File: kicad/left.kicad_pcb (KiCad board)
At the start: 4 copper layers, 127.3 x 89.6 mm, 139 parts, among them Q1 PMF170XP,115, Q2 FS8205A_C2830320, SW1 TS-1088-AR02016, U1 SN74LVC1G17DBVR, U2 E73-2G4M08S1C, U3 SN74LVC1G74DQER, U4 S2B-PH-K-S(LF)(SN), U5 BL8573CS8TR, U6 DW01A_C42380662, U7 LP5024RSMR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

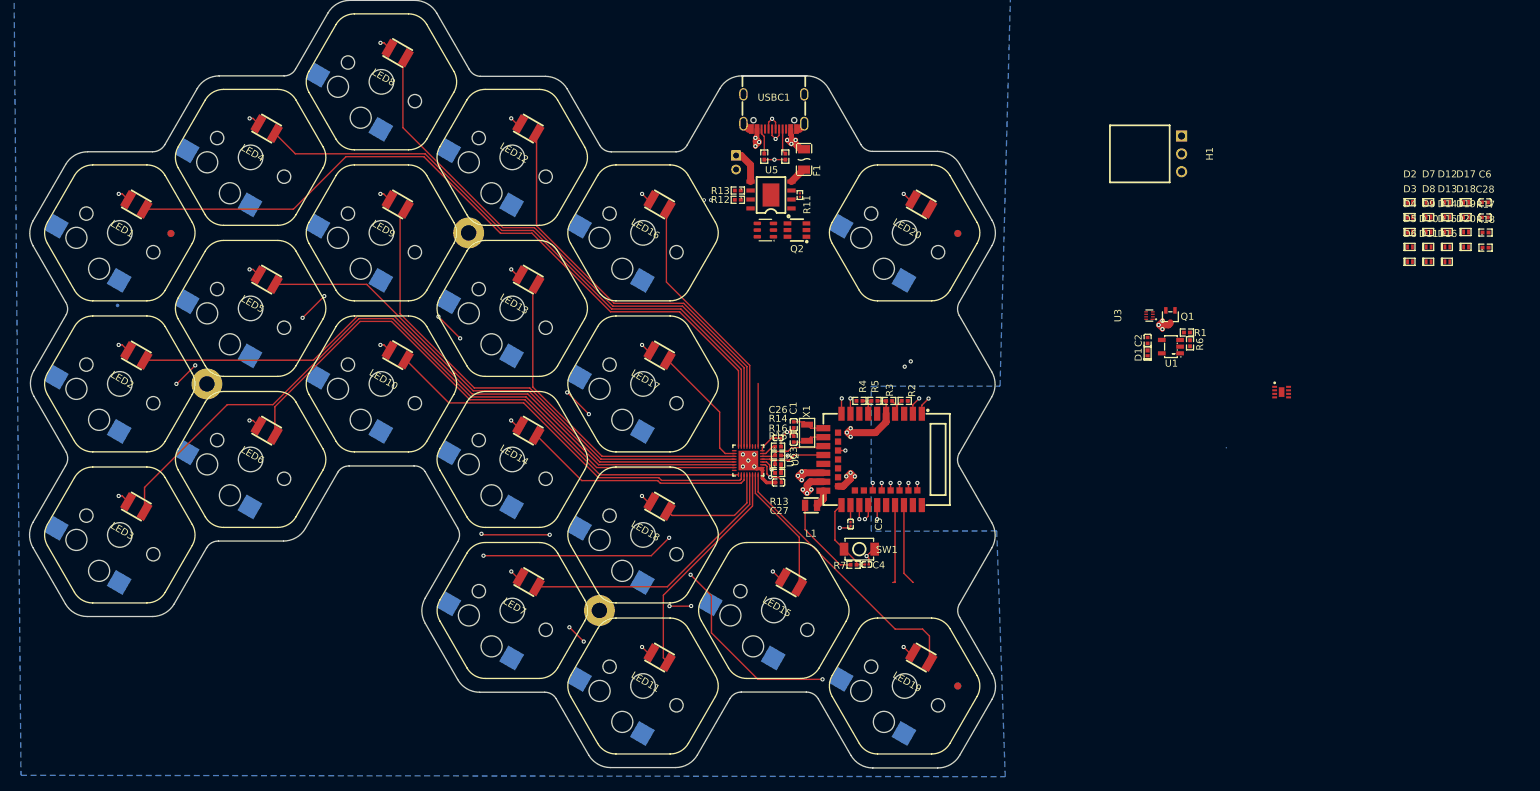
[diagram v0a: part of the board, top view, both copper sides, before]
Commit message: finished. needes inspection. added battery measurer. wired left side
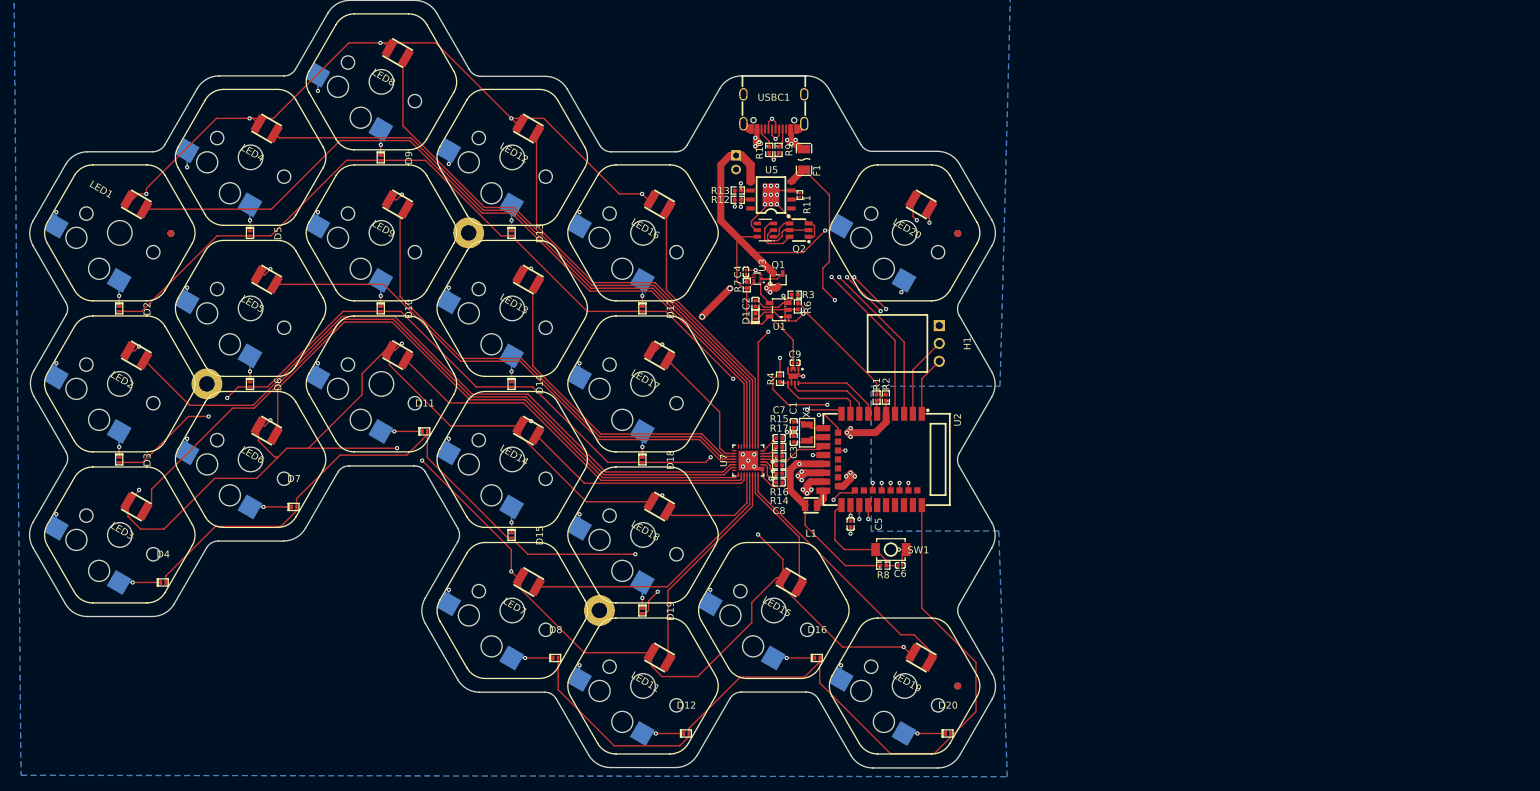
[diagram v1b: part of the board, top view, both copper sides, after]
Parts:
- removed C26: GRM033C71C104KE14D, easyeda2kicad:C0201
- removed C27, C28: GRM155C71C105KE11D, easyeda2kicad:C0402
- removed the R13 at (126.6, 83.1)
- removed R18: RC0402FR-0710KL, easyeda2kicad:R0402
- removed R5: RC0402FR-07100KL, easyeda2kicad:R0402
- added C7: GRM155C71C105KE11D, easyeda2kicad:C0402, F.Cu at (126.7, 78.1)
- added C8: GRM155C71C105KE11D, easyeda2kicad:C0402, F.Cu at (126.7, 84.4)
- added C9: GRM033C71C104KE14D, easyeda2kicad:C0201, F.Cu at (129.0, 67.4)
- added R10: RC0402FR-075K1L, easyeda2kicad:R0402, F.Cu at (125.3, 37.1)
- C5: footprint easyeda2kicad:C0201 -> easyeda2kicad:C0402
- C6: footprint easyeda2kicad:C0402 -> easyeda2kicad:C0201
- moved D3 187.0 mm to (32.8, 81.2), turned to -90 degrees
- moved D2 184.4 mm to (32.8, 59.7), turned to -90 degrees
- moved D4 184.3 mm to (39.1, 98.7)
- moved D7 167.2 mm to (57.7, 87.9)
- moved D6 166.0 mm to (51.4, 70.5), turned to -90 degrees
- moved D5 165.1 mm to (51.4, 49.0), turned to -90 degrees
- moved D9 149.5 mm to (70.0, 38.2), turned to -90 degrees
- moved D10 149.4 mm to (70.0, 59.7), turned to -90 degrees
- moved D11 144.9 mm to (76.3, 77.2)
- moved D15 139.4 mm to (88.6, 92.0), turned to -90 degrees
- moved D8 139.2 mm to (94.9, 109.4)
- moved D14 135.0 mm to (88.6, 70.5), turned to -90 degrees
- moved D13 133.2 mm to (88.6, 49.0), turned to -90 degrees
- moved D12 132.1 mm to (113.5, 120.2)
- moved D19 129.1 mm to (107.3, 102.7), turned to -90 degrees
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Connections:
- U2 pad 1: unconnected-(U2-P1.11-Pad1) -> /SWDIO
- U2 pad 10: /ROW2 -> /ROW1
- U2 pad 12: /ROW3 -> /ROW2
- U2 pad 18: /BAT_ALTR -> unconnected-(U2-AI2-Pad18)
- U2 pad 2: unconnected-(U2-P1.10-Pad2) -> /SWBCLK
- U2 pad 28: /ROW1 -> /ROW3
- U2 pad 3: unconnected-(U2-P0.03-Pad3) -> /STDBY
- U2 pad 30: /PWR_BTN_PRESS -> unconnected-(U2-P17-Pad30)
- U2 pad 32: /COL4 -> /COL5
- U2 pad 34: /COL3 -> /COL4
- U2 pad 36: /COL2 -> /COL3
- U2 pad 37: /SWDIO -> unconnected-(U2-SWD-Pad37)
- U2 pad 38: /COL1 -> /COL2
- U2 pad 39: /SWBCLK -> unconnected-(U2-SWC-Pad39)
- U2 pad 4: unconnected-(U2-AI4-Pad4) -> /CHRG
- U2 pad 40: unconnected-(U2-P1.04-Pad40) -> /COL1
- U2 pad 41: /CHRG -> unconnected-(U2-NF1-Pad41)
- U2 pad 43: /STDBY -> /ROW4
- U2 pad 6: /COL5 -> /PWR_BTN_PRESS
- U2 pad 7: unconnected-(U2-AI0-Pad7) -> /SDA_BAT
- U2 pad 8: unconnected-(U2-AI5-Pad8) -> /SCL_BAT
- U2 pad 9: /ROW4 -> /BAT_ALTR
- U7 pad 1: /LED19 -> /LED20
- U7 pad 10: /LED3 -> /LED17
- U7 pad 11: /LED2 -> /LED13
- U7 pad 12: /LED5 -> /LED9
- U7 pad 13: /LED9 -> /LED5
- U7 pad 14: /LED13 -> /LED2
- U7 pad 15: /LED17 -> /LED3
- U7 pad 17: /LED1 -> /LED6
- U7 pad 18: /LED4 -> /LED10
- U7 pad 19: /LED8 -> /LED14
- U7 pad 2: /LED15 -> /LED16
- U7 pad 20: /LED12 -> /LED18
- U7 pad 21: /LED16 -> /LED7
- U7 pad 22: /LED20 -> /LED11
- U7 pad 23: unconnected-(U7-OUT22-Pad23) -> /LED15
- U7 pad 24: unconnected-(U7-OUT23-Pad24) -> /LED19
- U7 pad 3: /LED11 -> /LED12
- U7 pad 4: /LED7 -> /LED8
- U7 pad 5: /LED18 -> /LED4
- U7 pad 6: /LED14 -> /LED1
- U7 pad 7: /LED10 -> unconnected-(U7-OUT6-Pad7)
- U7 pad 8: /LED6 -> unconnected-(U7-OUT7-Pad8)
- U8 pad 7: /SCL -> /SCL_BAT
- U8 pad 8: /SDA -> /SDA_BAT
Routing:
- net /PWR: track 47.6 -> 694.1 mm, vias 27 -> 30
- net /COL5: track 0.00 -> 184.1 mm, vias 0 -> 5
- net unconnected-(U2-P0.13-Pad33): track 135.4 -> 0.00 mm, vias 3 -> 0
- net /ROW3: track 0.00 -> 131.9 mm, vias 0 -> 3
- net unconnected-(U2-P1.04-Pad40): track 126.8 -> 0.00 mm, vias 3 -> 0
- net /ROW1: track 0.00 -> 126.7 mm, vias 0 -> 2
- net unconnected-(U2-P1.06-Pad42): track 109.7 -> 0.00 mm, vias 1 -> 0
- net /COL1: track 130.8 -> 228.3 mm, vias 3 -> 4
- net /COL2: track 166.7 -> 255.9 mm, vias 1 -> 5
- net /VDD_nRF: track 14.2 -> 87.9 mm, vias 1 -> 4
- net /COL3: track 164.0 -> 232.0 mm, vias 3 -> 5
- net /BAT+: track 5.00 -> 72.1 mm, vias 0 -> 1
- net /VBUS: track 4.50 -> 68.4 mm, vias 0 -> 2
- net /ROW4: track 177.6 -> 116.6 mm, vias 1 -> 0
- net /LED20: track 2.35 -> 51.7 mm, vias 0 -> 2
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
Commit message: changed on/off timing resistor to 2M61 0805
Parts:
- removed R6: 0402WGF1604TCE, easyeda2kicad:R0402
- added R5: RC0805FR-072M61L, easyeda2kicad:R0805, F.Cu at (131.2, 60.9)
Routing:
- net GND: track 85.3 -> 81.0 mm, vias 30 -> 31
- net Net-(U1-A): track 6.99 -> 9.84 mm
- net /PWR_BTN: track 44.6 -> 46.8 mm

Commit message: added gnd vias all over the board. went trough schematic again. changed resistor for rc to bigger one in footprint, and smaller one in Ohm. both left and right sides are ready. just need to go over the kicads check and lastly let someone on discord have a look on the project
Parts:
- removed Fi4, Fi5: Fiducial_1mm_Mask2mm, Fiducial:Fiducial_1mm_Mask2mm
- removed Fi6: Fiducial_1mm_Mask2mm, 
- removed G*** (x2): LOGO, images:monster
- removed R15: RT0402BRD0737K4L, easyeda2kicad:R0402
- added BAT+: TestPoint_Pad_D1.5mm, TestPoint:TestPoint_Pad_D1.5mm, F.Cu at (118.3, 36.1)
- added GND: TestPoint_Pad_D1.5mm, TestPoint:TestPoint_Pad_D1.5mm, F.Cu at (116.5, 39.6)
- added PWR: TestPoint_Pad_D1.5mm, TestPoint:TestPoint_Pad_D1.5mm, F.Cu at (116.6, 57.6)
- added R6: ERA2AED753X, easyeda2kicad:R0402, F.Cu at (126.7, 79.4)
- added VBUS: TestPoint_Pad_D1.5mm, TestPoint:TestPoint_Pad_D1.5mm, F.Cu at (134.6, 40.1)
- added VDD_nrf: TestPoint_Pad_D1.5mm, TestPoint:TestPoint_Pad_D1.5mm, F.Cu at (126.0, 65.0)
- G**: moved to B.Cu
- moved G** 296.4 mm to (127.1, 68.4), turned to 180 degrees
- moved Fi2 2.00 mm to (42.2, 49.0)
- moved Fi1 1.00 mm to (153.2, 49.0)
- moved Fi3 1.00 mm to (153.2, 113.4)
- moved D1 0.19 mm to (123.4, 61.0)
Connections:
- U6 pad 5: GND -> /BAT+
- U6 pad 6: /BAT+ -> GND
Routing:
- net /PWR: track 694.1 -> 701.5 mm
- net GND: track 81.0 -> 85.5 mm, vias 31 -> 97
- net /VBUS: track 68.4 -> 72.8 mm
- net /BAT+: track 72.1 -> 75.6 mm
- net /VDD_nRF: track 87.9 -> 90.4 mm
- net /LED1: track 112.7 -> 115.0 mm
- net /COL2: track 255.9 -> 257.7 mm
- net /COL1: track 228.3 -> 229.5 mm
- net /COL3: track 232.0 -> 233.2 mm
- net /LED12: track 62.5 -> 61.8 mm
- net /LED3: track 106.1 -> 105.5 mm
- net /LED2: track 101.4 -> 100.9 mm

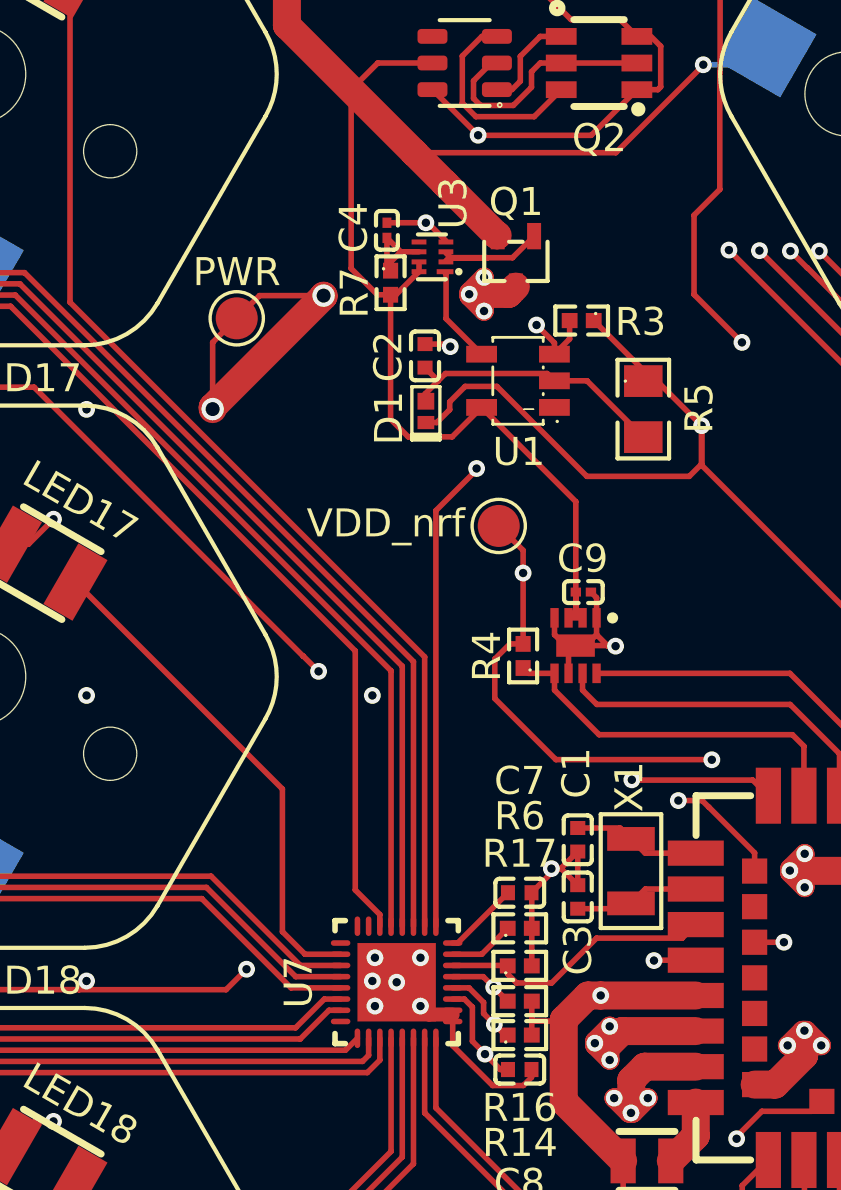
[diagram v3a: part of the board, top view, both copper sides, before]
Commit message: update vias under led controller... on left part. checking correctness of footprints in progress
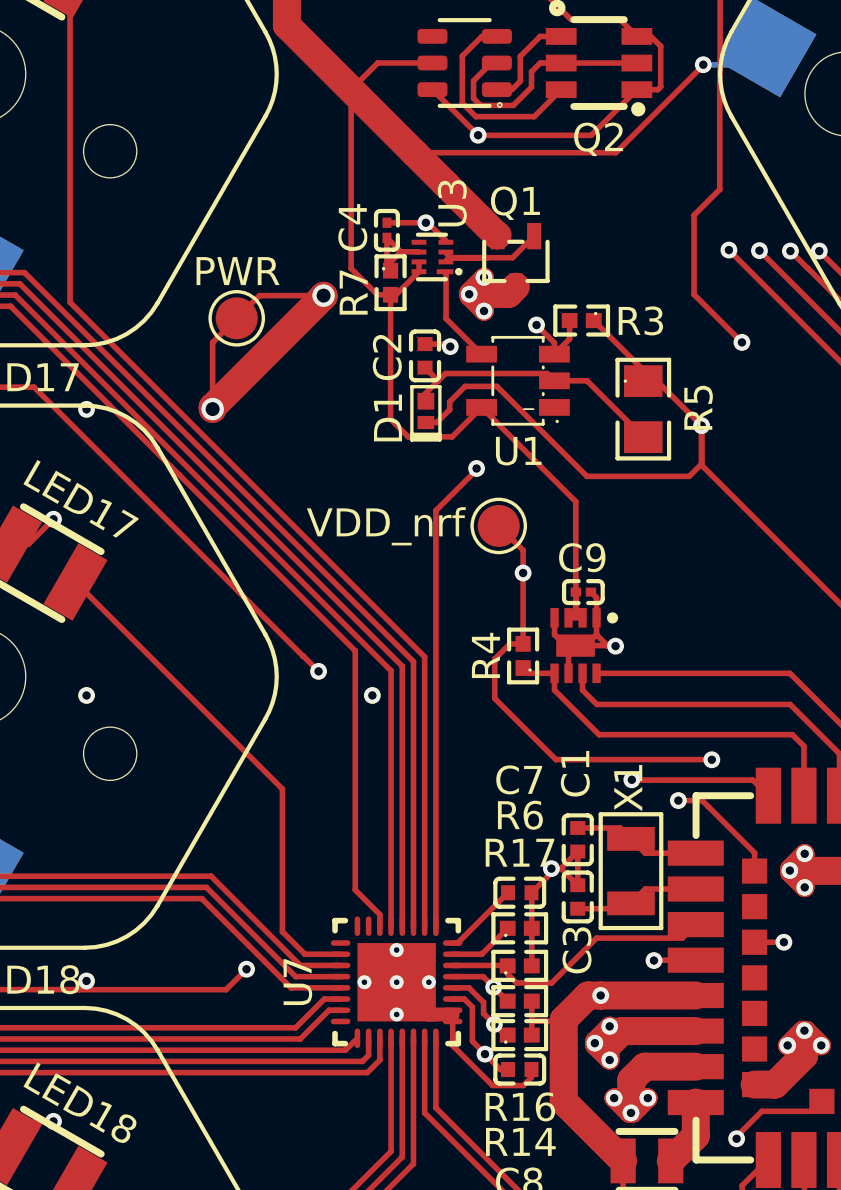
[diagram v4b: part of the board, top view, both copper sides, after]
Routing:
- net GND: vias 97 -> 96
